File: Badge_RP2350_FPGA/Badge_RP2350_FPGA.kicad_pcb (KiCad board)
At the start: 2 copper layers, 105 parts, among them J1 USB_C_Receptacle_USB2.0_16P, J2 Conn_01x03_Pin, J4 SM03B-SRSS-TB, SW1 SW_Push, SW12 On/Off, SW2 SW_Push, U1 RP2350_60QFN, U2 GW1N-LV9QN88C6_I5_, U3 ME6211C12, U4 TMI7003C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

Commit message: started PCB layout
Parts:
- moved C40 154.2 mm to (62.0, 192.0)
- moved C43 152.6 mm to (70.0, 191.0)
- moved C44 152.6 mm to (70.0, 195.8)
- moved C41 147.6 mm to (62.0, 187.0)
- moved C5 138.2 mm to (77.0, 191.0)
- moved C42 137.6 mm to (71.0, 187.0)
- moved L2 133.9 mm to (88.0, 196.0)
- moved C46 131.8 mm to (115.0, 196.0)
- moved L3 130.0 mm to (83.0, 195.0)
- moved L4 129.5 mm to (75.0, 195.0)
- moved U3 120.1 mm to (110.5, 187.3)
- moved U4 115.0 mm to (113.7, 192.0)
- moved C45 112.8 mm to (124.0, 193.0)
- moved L1 110.6 mm to (68.0, 146.0)
- moved R4 99.9 mm to (59.7, 149.3)
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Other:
- board outline added: 100 x 150 mm

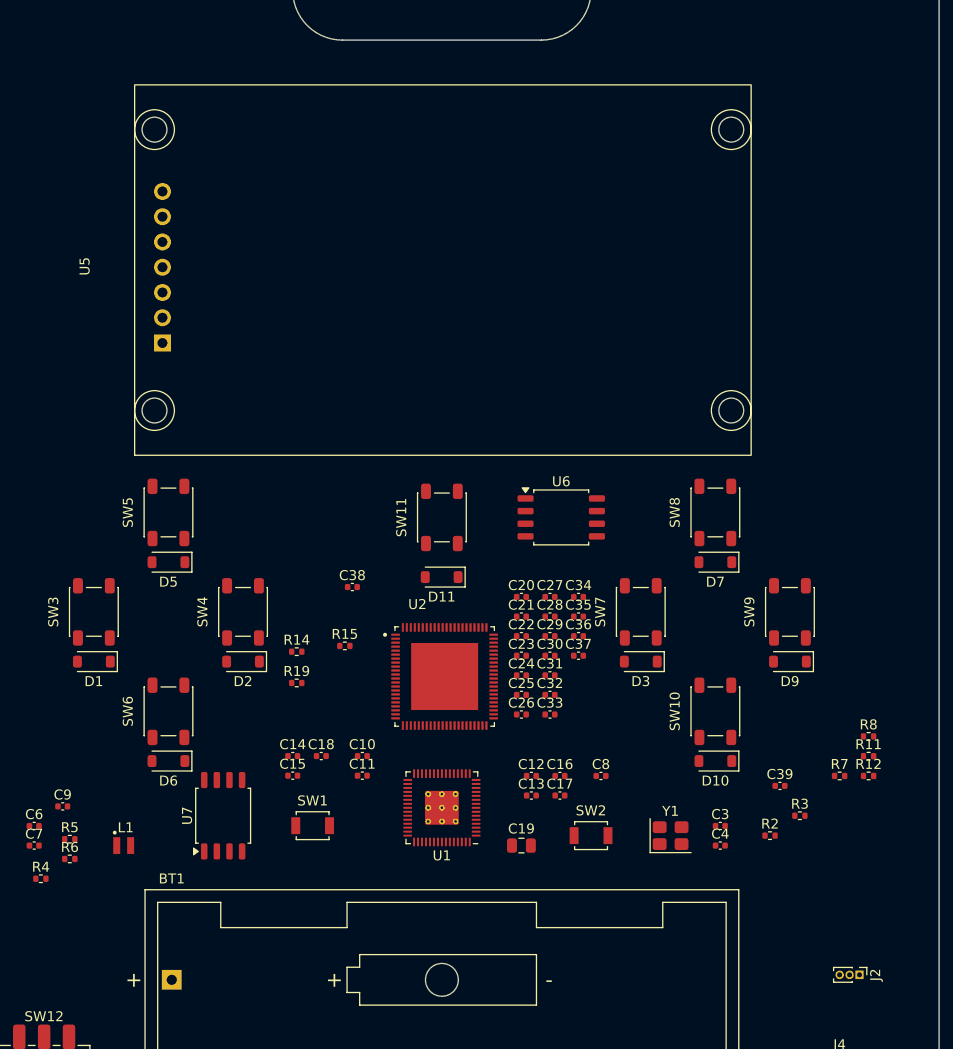
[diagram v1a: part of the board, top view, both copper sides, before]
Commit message: add headers and fix voltage references
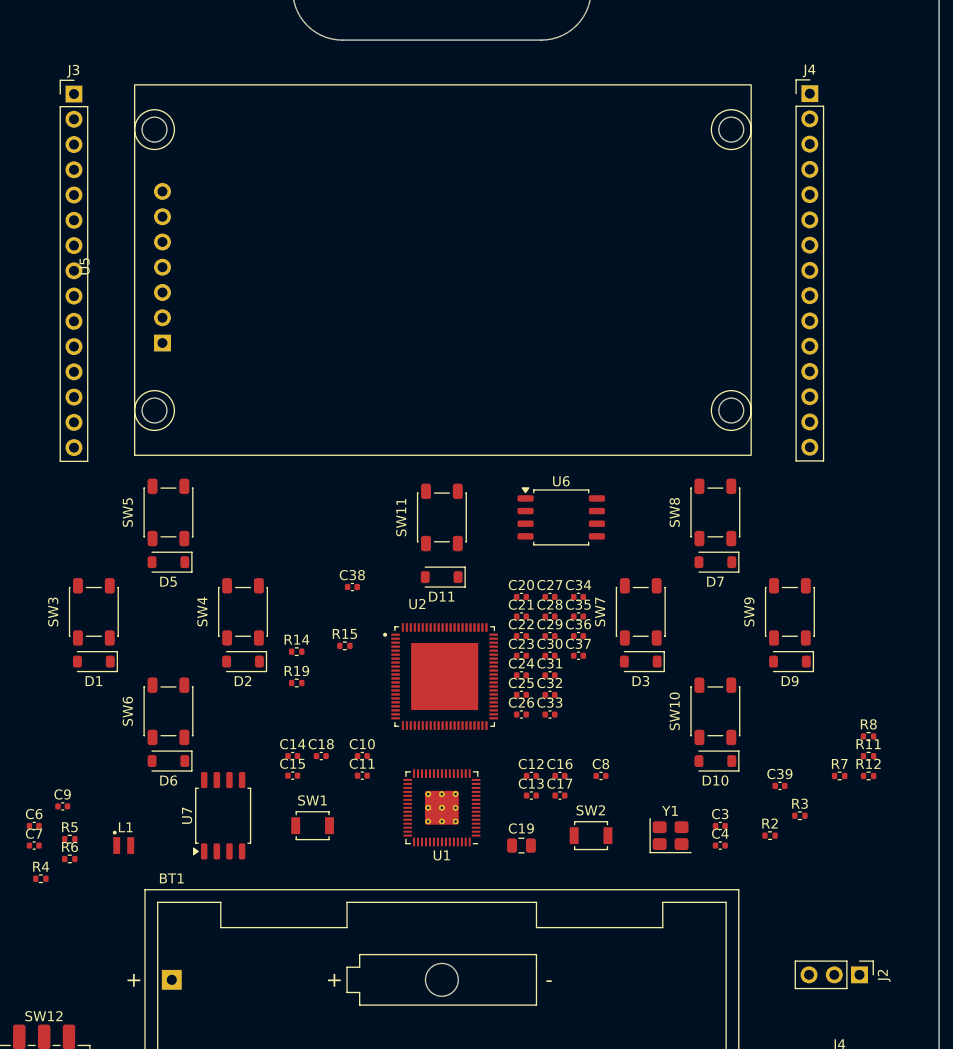
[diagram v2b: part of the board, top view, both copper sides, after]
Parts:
- added J3: Conn_01x15_Pin, Connector_PinHeader_2.54mm:PinHeader_1x15_P2.54mm_Vertical, F.Cu at (63.0, 70.4)
- added J4: Conn_01x15_Pin, Connector_PinHeader_2.54mm:PinHeader_1x15_P2.54mm_Vertical, F.Cu at (137.0, 70.4)
- J2: footprint Connector_PinHeader_1.00mm:PinHeader_1x03_P1.00mm_Vertical -> Connector_PinHeader_2.54mm:PinHeader_1x03_P2.54mm_Vertical
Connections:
- net /RP2350A/GPIO0 renamed GPIO0
- C10 pad 1: +1V1 -> +1v1
- C11 pad 1: +1V1 -> +1v1
- C12 pad 1: +3V3 -> + 3v3
- C13 pad 1: +3V3 -> + 3v3
- C14 pad 1: +3V3 -> + 3v3
- C15 pad 1: +3V3 -> + 3v3
- C16 pad 1: +3V3 -> + 3v3
- C17 pad 1: +3V3 -> + 3v3
- C18 pad 1: +3V3 -> + 3v3
- C19 pad 1: +3V3 -> + 3v3
- C38 pad 1: +3V3 -> VCC00_1_2_3V3
- C40 pad 1: +3V3 -> + 3v3
- C43 pad 1: +3V3 -> + 3v3
- C6 pad 1: +3V3 -> + 3v3
- C8 pad 1: +1V1 -> +1v1
- L3 pad 1: +3V3 -> + 3v3
- R10 pad 1: +3V3 -> + 3v3
- R5 pad 1: +3V3 -> + 3v3
- U1 pad 1: +3V3 -> + 3v3
- U1 pad 11: +3V3 -> + 3v3
- U1 pad 17: /RP2350A/GPIO13 -> GPIO13
- U1 pad 20: +3V3 -> + 3v3
- U1 pad 23: +1V1 -> +1v1
- U1 pad 3: /RP2350A/GPIO1 -> GPIO1
- U1 pad 30: +3V3 -> + 3v3
- U1 pad 38: +3V3 -> + 3v3
- U1 pad 39: +1V1 -> +1v1
- U1 pad 4: /RP2350A/GPIO2 -> GPIO2
- U1 pad 40: /RP2350A/GPIO26_ADC0 -> GPIO26_ADC0
- U1 pad 41: /RP2350A/GPIO27_ADC1 -> GPIO27_ADC1
- U1 pad 42: /RP2350A/GPIO28_ADC2 -> GPIO28_ADC2
- U1 pad 43: /RP2350A/GPIO29_ADC3 -> GPIO29_ADC3
- U1 pad 44: +3V3 -> + 3v3
- U1 pad 45: +3V3 -> + 3v3
- U1 pad 49: +3V3 -> + 3v3
- U1 pad 5: /RP2350A/GPIO3 -> GPIO3
- U1 pad 53: +3V3 -> + 3v3
- U1 pad 54: +3V3 -> + 3v3
- U1 pad 6: +1V1 -> +1v1
- U1 pad 7: /RP2350A/GPIO4 -> GPIO4
- U1 pad 8: /RP2350A/GPIO5 -> GPIO5
- U2 pad 10: unconnected-(U2-IOL14A/DONE-Pad10) -> L14A
- U2 pad 11: unconnected-(U2-IOL15A/GCLKT_6-Pad11) -> L15A
- U2 pad 13: unconnected-(U2-IOL22A-Pad13) -> L22A
- U2 pad 14: unconnected-(U2-IOL22B-Pad14) -> L22B
- U2 pad 27: unconnected-(U2-IOB11A-Pad27) -> B11A
- U2 pad 28: unconnected-(U2-IOB11B-Pad28) -> B11B
- U2 pad 29: unconnected-(U2-IOB13A-Pad29) -> B13A
- U2 pad 30: unconnected-(U2-IOB13B-Pad30) -> B13B
- U2 pad 85: unconnected-(U2-IOT8B-Pad85) -> T8B
- U2 pad 86: unconnected-(U2-IOT8A-Pad86) -> T8A
- U2 pad 9: unconnected-(U2-IOL13B/RECONFIG_N-Pad9) -> L13B
- U6 pad 8: +3V3 -> VCC00_1_2_3V3

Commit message: add x to unused pins and connect more pins
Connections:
- U2 pad 31: unconnected-(U2-IOB17A-Pad31) -> B17A
- U2 pad 32: unconnected-(U2-IOB17B-Pad32) -> B17B
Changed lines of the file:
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@@
 			(net "unconnected-(U2-IOL2A-Pad3)")
 			(pinfunction "IOL2A_3")
-			(pintype "bidirectional")
+			(pintype "bidirectional+no_connect")
 			(solder_mask_margin 0.102)
 		)
@@
 			(net "unconnected-(U2-IOL5A{slash}JTAGSEL_N{slash}LPLL_T_IN-Pad4)")
 			(pinfunction "IOL5A/JTAGSEL_N/LPLL_T_IN_4")
-			(pintype "bidirectional")
+			(pintype "bidirectional+no_connect")
 			(solder_mask_margin 0.102)
 		)
@@
 			(net "unconnected-(U2-IOL26A-Pad15)")
 			(pinfunction "IOL26A_15")
-			(pintype "bidirectional")
+			(pintype "bidirectional+no_connect")
 			(solder_mask_margin 0.102)
 		)
@@
 			(net "unconnected-(U2-IOL26B-Pad16)")
 			(pinfunction "IOL26B_16")
-			(pintype "bidirectional")
+			(pintype "bidirectional+no_connect")
 			(solder_mask_margin 0.102)
 		)
@@
 			(net "unconnected-(U2-IOB2A-Pad17)")
 			(pinfunction "IOB2A_17")
-			(pintype "bidirectional")
+			(pintype "bidirectional+no_connect")
 			(solder_mask_margin 0.102)
 		)
@@
 			(net "unconnected-(U2-IOB2B-Pad18)")
 			(pinfunction "IOB2B_18")
-			(pintype "bidirectional")
+			(pintype "bidirectional+no_connect")
 			(solder_mask_margin 0.102)
 		)
@@
 			(net "unconnected-(U2-IOB4A-Pad19)")
 			(pinfunction "IOB4A_19")
-			(pintype "bidirectional")
+			(pintype "bidirectional+no_connect")
 			(solder_mask_margin 0.102)
 		)
@@
 			(net "unconnected-(U2-IOB4B-Pad20)")
 			(pinfunction "IOB4B_20")
-			(pintype "bidirectional")
+			(pintype "bidirectional+no_connect")
 			(solder_mask_margin 0.102)
 		)
@@
 			(layers "F.Cu" "F.Mask" "F.Paste")
 			(roundrect_rratio 0.125)
-			(net "unconnected-(U2-IOB17A-Pad31)")
+			(net "B17A")
 			(pinfunction "IOB17A_31")
 			(pintype "bidirectional")
@@
 			(layers "F.Cu" "F.Mask" "F.Paste")
 			(roundrect_rratio 0.125)
-			(net "unconnected-(U2-IOB17B-Pad32)")
+			(net "B17B")
 			(pinfunction "IOB17B_32")
 			(pintype "bidirectional")
@@
 			(net "unconnected-(U2-IOB23A-Pad33)")
 			(pinfunction "IOB23A_33")
-			(pintype "bidirectional")
+			(pintype "bidirectional+no_connect")
 			(solder_mask_margin 0.102)
 		)
@@
 			(net "unconnected-(U2-IOB23B-Pad34)")
 			(pinfunction "IOB23B_34")
-			(pintype "bidirectional")
+			(pintype "bidirectional+no_connect")
 			(solder_mask_margin 0.102)
 		)
@@
 			(net "unconnected-(U2-IOB29A{slash}GCLKT_4-Pad35)")
 			(pinfunction "IOB29A/GCLKT_4_35")
-			(pintype "bidirectional")
+			(pintype "bidirectional+no_connect")
 			(solder_mask_margin 0.102)
 		)
@@
 			(net "unconnected-(U2-IOB29B{slash}GCLKC_4-Pad36)")
 			(pinfunction "IOB29B/GCLKC_4_36")
-			(pintype "bidirectional")
+			(pintype "bidirectional+no_connect")
 			(solder_mask_margin 0.102)
 		)
@@
 			(net "unconnected-(U2-IOB31A-Pad37)")
 			(pinfunction "IOB31A_37")
-			(pintype "bidirectional")
+			(pintype "bidirectional+no_connect")
 			(solder_mask_margin 0.102)
 		)
@@
 			(net "unconnected-(U2-IOB31B-Pad38)")
 			(pinfunction "IOB31B_38")
-			(pintype "bidirectional")
+			(pintype "bidirectional+no_connect")
 			(solder_mask_margin 0.102)
 		)
@@
 			(net "unconnected-(U2-IOB33A-Pad39)")
 			(pinfunction "IOB33A_39")
-			(pintype "bidirectional")
+			(pintype "bidirectional+no_connect")
 			(solder_mask_margin 0.102)
 		)
@@
 			(net "unconnected-(U2-IOB33B-Pad40)")
 			(pinfunction "IOB33B_40")
-			(pintype "bidirectional")
+			(pintype "bidirectional+no_connect")
 			(solder_mask_margin 0.102)
 		)
@@
 			(net "unconnected-(U2-IOB41A-Pad41)")
 			(pinfunction "IOB41A_41")
-			(pintype "bidirectional")
+			(pintype "bidirectional+no_connect")
 			(solder_mask_margin 0.102)
 		)
@@
 			(net "unconnected-(U2-IOB41B-Pad42)")
 			(pinfunction "IOB41B_42")
-			(pintype "bidirectional")
+			(pintype "bidirectional+no_connect")
 			(solder_mask_margin 0.102)
 		)
@@
 			(net "unconnected-(U2-IOB43B-Pad47)")
 			(pinfunction "IOB43B_47")
-			(pintype "bidirectional")
+			(pintype "bidirectional+no_connect")
 			(solder_mask_margin 0.102)
 		)
@@
 			(net "unconnected-(U2-IOR24B-Pad48)")
 			(pinfunction "IOR24B_48")
-			(pintype "bidirectional")
+			(pintype "bidirectional+no_connect")
 			(solder_mask_margin 0.102)
 		)
@@
 			(net "unconnected-(U2-IOR24A-Pad49)")
 			(pinfunction "IOR24A_49")
-			(pintype "bidirectional")
+			(pintype "bidirectional+no_connect")
 			(solder_mask_margin 0.102)
 		)
@@
 			(net "unconnected-(U2-IOR22B-Pad50)")
 			(pinfunction "IOR22B_50")
-			(pintype "bidirectional")
+			(pintype "bidirectional+no_connect")
 			(solder_mask_margin 0.102)
 		)
@@
 			(net "unconnected-(U2-IOR17B{slash}GCLKC_3-Pad51)")
 			(pinfunction "IOR17B/GCLKC_3_51")
-			(pintype "bidirectional")
+			(pintype "bidirectional+no_connect")
 			(solder_mask_margin 0.102)
 		)
@@
 			(net "unconnected-(U2-IOR17A{slash}GCLKT_3-Pad52)")
 			(pinfunction "IOR17A/GCLKT_3_52")
-			(pintype "bidirectional")
+			(pintype "bidirectional+no_connect")
 			(solder_mask_margin 0.102)
 		)
@@
 			(net "unconnected-(U2-IOR15B{slash}DOUT{slash}WE_N-Pad53)")
 			(pinfunction "IOR15B/DOUT/WE_N_53")
-			(pintype "bidirectional")
+			(pintype "bidirectional+no_connect")
 			(solder_mask_margin 0.102)
 		)
@@
 			(net "unconnected-(U2-IOR15A{slash}DIN{slash}CLKHOLD_N-Pad54)")
 			(pinfunction "IOR15A/DIN/CLKHOLD_N_54")
-			(pintype "bidirectional")
+			(pintype "bidirectional+no_connect")
 			(solder_mask_margin 0.102)
 		)
@@
 			(net "unconnected-(U2-IOR14B{slash}SSPI_CS_N{slash}D0-Pad55)")
 			(pinfunction "IOR14B/SSPI_CS_N/D0_55")
-			(pintype "bidirectional")
+			(pintype "bidirectional+no_connect")
 			(solder_mask_margin 0.102)
 		)
@@
 			(net "unconnected-(U2-IOR14A{slash}SO{slash}D1-Pad56)")
 			(pinfunction "IOR14A/SO/D1_56")
-			(pintype "bidirectional")
+			(pintype "bidirectional+no_connect")
 			(solder_mask_margin 0.102)
 		)
@@
 			(net "unconnected-(U2-IOR13A{slash}FASTRD_N{slash}D3-Pad57)")
 			(pinfunction "IOR13A/FASTRD_N/D3_57")
-			(pintype "bidirectional")
+			(pintype "bidirectional+no_connect")
 			(solder_mask_margin 0.102)
 		)
@@
 			(net "unconnected-(U2-IOR5A{slash}RPLL_T_IN-Pad63)")
 			(pinfunction "IOR5A/RPLL_T_IN_63")
-			(pintype "bidirectional")
+			(pintype "bidirectional+no_connect")
 			(solder_mask_margin 0.102)
 		)
@@
 			(net "unconnected-(U2-IOT42B-Pad68)")
 			(pinfunction "IOT42B_68")
-			(pintype "bidirectional")
+			(pintype "bidirectional+no_connect")
 			(solder_mask_margin 0.102)
 		)
@@
 			(net "unconnected-(U2-IOT42A-Pad69)")
 			(pinfunction "IOT42A_69")
-			(pintype "bidirectional")
+			(pintype "bidirectional+no_connect")
 			(solder_mask_margin 0.102)
 		)
@@
 			(net "unconnected-(U2-IOT41B-Pad70)")
 			(pinfunction "IOT41B_70")
-			(pintype "bidirectional")
+			(pintype "bidirectional+no_connect")
 			(solder_mask_margin 0.102)
 		)
@@
 			(net "unconnected-(U2-IOT41A-Pad71)")
 			(pinfunction "IOT41A_71")
-			(pintype "bidirectional")
+			(pintype "bidirectional+no_connect")
 			(solder_mask_margin 0.102)
 		)
@@
 			(net "unconnected-(U2-IOT39B-Pad72)")
 			(pinfunction "IOT39B_72")
-			(pintype "bidirectional")
+			(pintype "bidirectional+no_connect")
 			(solder_mask_margin 0.102)
 		)
@@
 			(net "unconnected-(U2-IOT39A-Pad73)")
 			(pinfunction "IOT39A_73")
-			(pintype "bidirectional")
+			(pintype "bidirectional+no_connect")
 			(solder_mask_margin 0.102)
 		)
@@
 			(net "unconnected-(U2-IOT38B-Pad74)")
 			(pinfunction "IOT38B_74")
-			(pintype "bidirectional")
+			(pintype "bidirectional+no_connect")
 			(solder_mask_margin 0.102)
 		)
@@
 			(net "unconnected-(U2-IOT38A-Pad75)")
 			(pinfunction "IOT38A_75")
-			(pintype "bidirectional")
+			(pintype "bidirectional+no_connect")
 			(solder_mask_margin 0.102)
 		)
@@
 			(net "unconnected-(U2-IOT37B-Pad76)")
 			(pinfunction "IOT37B_76")
-			(pintype "bidirectional")
+			(pintype "bidirectional+no_connect")
 			(solder_mask_margin 0.102)
 		)
@@
 			(net "unconnected-(U2-IOT37A-Pad77)")
 			(pinfunction "IOT37A_77")
-			(pintype "bidirectional")
+			(pintype "bidirectional+no_connect")
 			(solder_mask_margin 0.102)
 		)
@@
 			(net "unconnected-(U2-IOT12B-Pad79)")
 			(pinfunction "IOT12B_79")
-			(pintype "bidirectional")
+			(pintype "bidirectional+no_connect")
 			(solder_mask_margin 0.102)
 		)
@@
 			(net "unconnected-(U2-IOT12A-Pad80)")
 			(pinfunction "IOT12A_80")
-			(pintype "bidirectional")
+			(pintype "bidirectional+no_connect")
 			(solder_mask_margin 0.102)
 		)
@@
 			(net "unconnected-(U2-IOT11B-Pad81)")
 			(pinfunction "IOT11B_81")
-			(pintype "bidirectional")
+			(pintype "bidirectional+no_connect")
 			(solder_mask_margin 0.102)
 		)
@@
 			(net "unconnected-(U2-IOT11A-Pad82)")
 			(pinfunction "IOT11A_82")
-			(pintype "bidirectional")
+			(pintype "bidirectional+no_connect")
 			(solder_mask_margin 0.102)
 		)
@@
 			(net "unconnected-(U2-IOT10B-Pad83)")
 			(pinfunction "IOT10B_83")
-			(pintype "bidirectional")
+			(pintype "bidirectional+no_connect")
 			(solder_mask_margin 0.102)
 		)
@@
 			(net "unconnected-(U2-IOT10A-Pad84)")
 			(pinfunction "IOT10A_84")
-			(pintype "bidirectional")
+			(pintype "bidirectional+no_connect")
 			(solder_mask_margin 0.102)
 		)
@@
 			(net "unconnected-(U2-EXP-Pad89)")
 			(pinfunction "EXP_89")
-			(pintype "power_in")
-			(solder_mask_margin 0.102)
-		)
+			(pintype "power_in+no_connect")
+			(solder_mask_margin 0.102)
+		)

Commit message: almost finished component placement
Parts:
- removed the J4 at (140.0, 170.0)
- BT1: moved to B.Cu
- moved J2 66.4 mm to (97.5, 109.8), turned to 90 degrees
- moved SW12 58.6 mm to (112.2, 194.6)
- moved C48 58.4 mm to (86.8, 194.5)
- moved C47 58.1 mm to (88.7, 197.0)
- moved U6 57.2 mm to (99.9, 168.9)
- moved C1 54.4 mm to (86.8, 195.8), turned to 180 degrees
- moved BT1 54.3 mm to (127.1, 161.3), turned to 180 degrees
- moved C38 49.2 mm to (105.8, 166.9)
- moved C2 48.3 mm to (92.7, 195.8)
- moved R16 46.7 mm to (103.7, 186.5), turned to -90 degrees
- moved R14 46.2 mm to (105.8, 168.0), turned to 180 degrees
- moved C39 45.8 mm to (94.6, 116.7), turned to 90 degrees
- moved R12 43.2 mm to (105.5, 117.3), turned to 90 degrees
- moved R11 41.3 mm to (106.6, 117.3), turned to 90 degrees
- moved R15 41.3 mm to (94.0, 167.0)
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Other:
- outline, holes or cut-outs redrawn
